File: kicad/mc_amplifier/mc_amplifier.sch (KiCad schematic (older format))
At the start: 19 parts

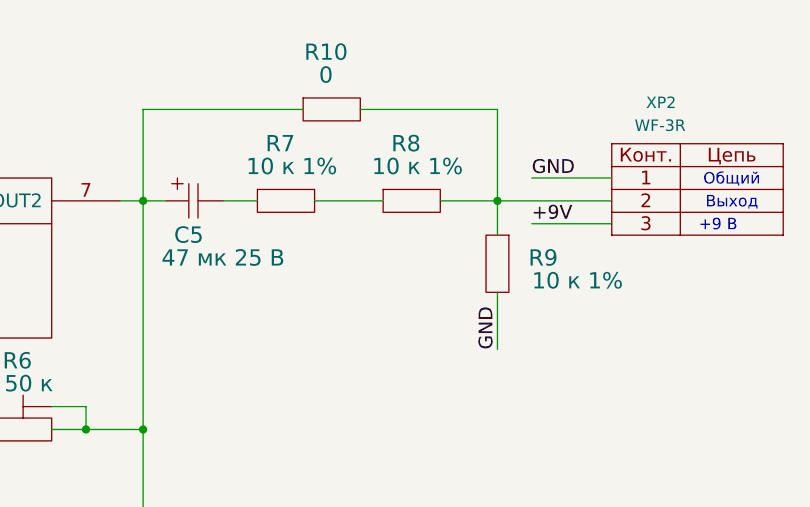
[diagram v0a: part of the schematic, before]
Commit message: Порпвил схему и отравил плату mc_amplifier rev1 на изготовление.
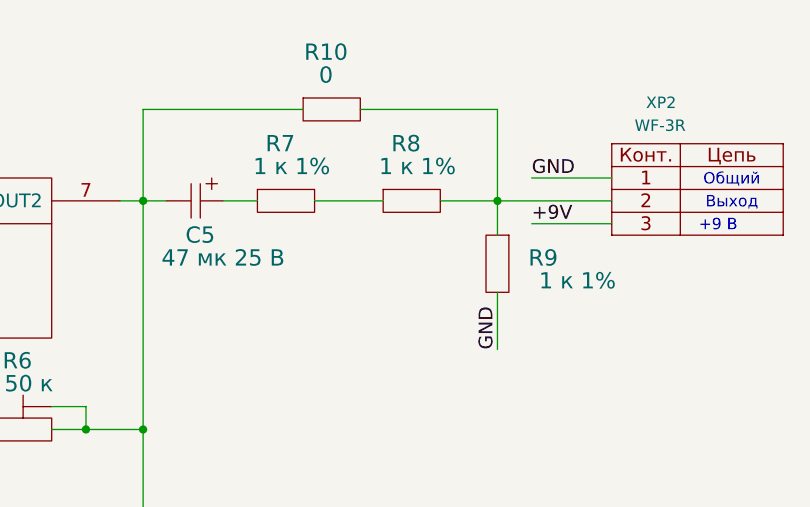
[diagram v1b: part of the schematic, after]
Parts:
- R7, R8, R9: value 10 к 1% -> 1 к 1%
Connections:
- net at C3.1, DA1.7 (OUT2), R10.1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: now also C5.2; no longer C5.1
- net at R7.1: now also C5.1; no longer C5.2
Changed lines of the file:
@@
 L LFcapitors:CAPITORS_ELECTROLYTIC C5
 U 1 1 5DDF39DE
-P 7700 2250
-F 0 "C5" H 7800 2100 71  0000 C CNN
+P 7950 2250
+F 0 "C5" H 8050 2100 71  0000 C CNN
 F 1 "47 мк 25 В" H 7950 2000 71  0000 C CNN
-F 2 "IWsmd_case:CASE_D" H 7700 2250 60  0001 C CNN
-F 3 "" H 7700 2250 60  0000 C CNN
-	1    7700 2250
-	1    0    0    -1
+F 2 "IWsmd_case:CASE_D" H 7950 2250 60  0001 C CNN
+F 3 "" H 7950 2250 60  0000 C CNN
+	1    7950 2250
+	-1   0    0    -1
 $EndComp
 Wire Wire Line
@@
 P 8100 2250
 F 0 "R7" H 8200 2500 71  0000 C CNN
-F 1 "10 к 1%" H 8250 2400 71  0000 C CNN
+F 1 "1 к 1%" H 8250 2400 71  0000 C CNN
 F 2 "IWsmd_case:SMD0805" H 8100 2250 60  0001 C CNN
 F 3 "" H 8225 2481 60  0000 C CNN
@@
 P 8650 2250
 F 0 "R8" H 8750 2500 71  0000 C CNN
-F 1 "10 к 1%" H 8800 2400 71  0000 C CNN
+F 1 "1 к 1%" H 8800 2400 71  0000 C CNN
 F 2 "IWsmd_case:SMD0805" H 8650 2250 60  0001 C CNN
 F 3 "" H 8775 2481 60  0000 C CNN
@@
 P 9150 2400
 F 0 "R9" V 9250 2600 71  0000 C CNN
-F 1 "10 к 1%" V 9350 2750 71  0000 C CNN
+F 1 "1 к 1%" V 9350 2750 71  0000 C CNN
 F 2 "IWsmd_case:SMD0805" H 9150 2400 60  0001 C CNN
 F 3 "" H 9150 2400 60  0000 C CNN

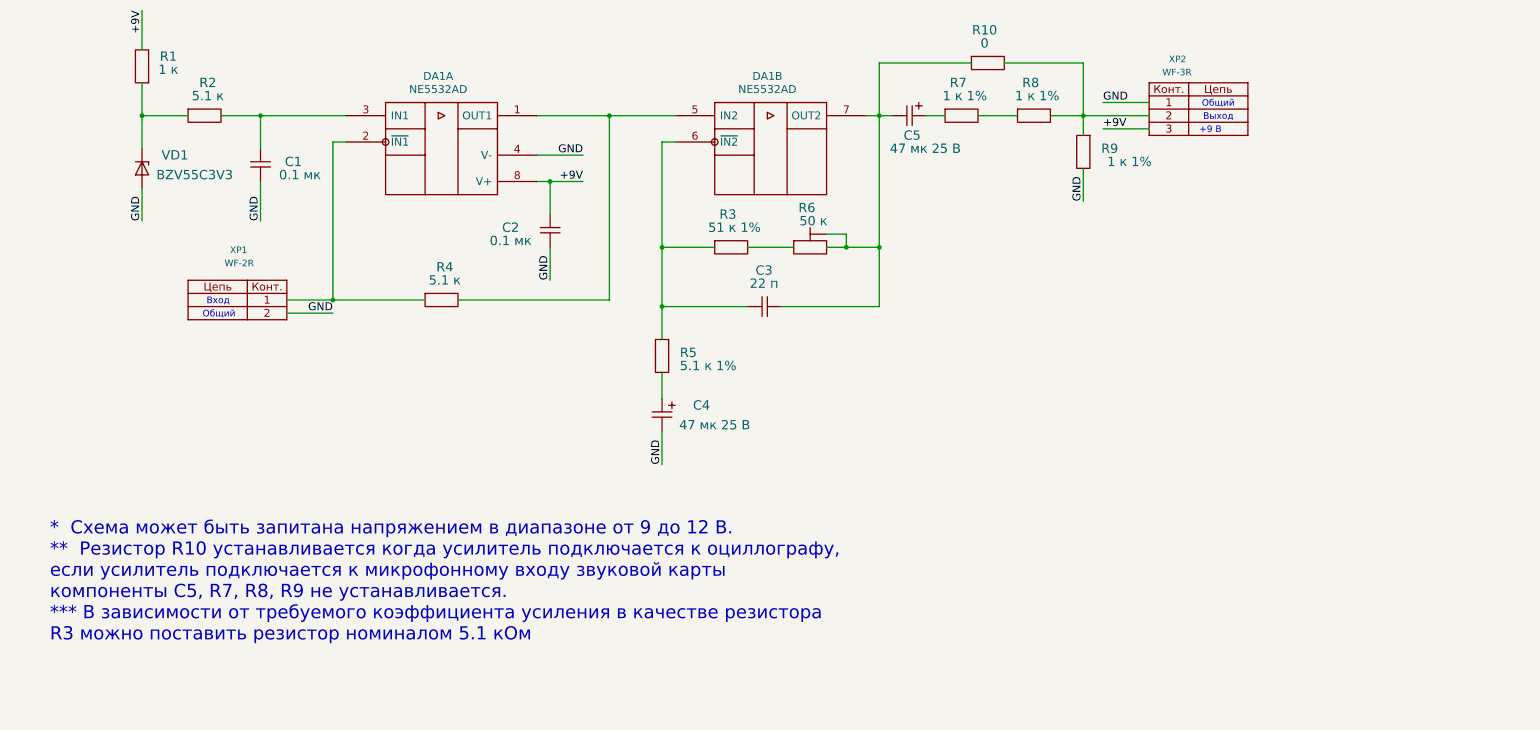
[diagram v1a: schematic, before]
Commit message: Поправил схему и отравил плату mc_amplifier rev1 на изготовление.
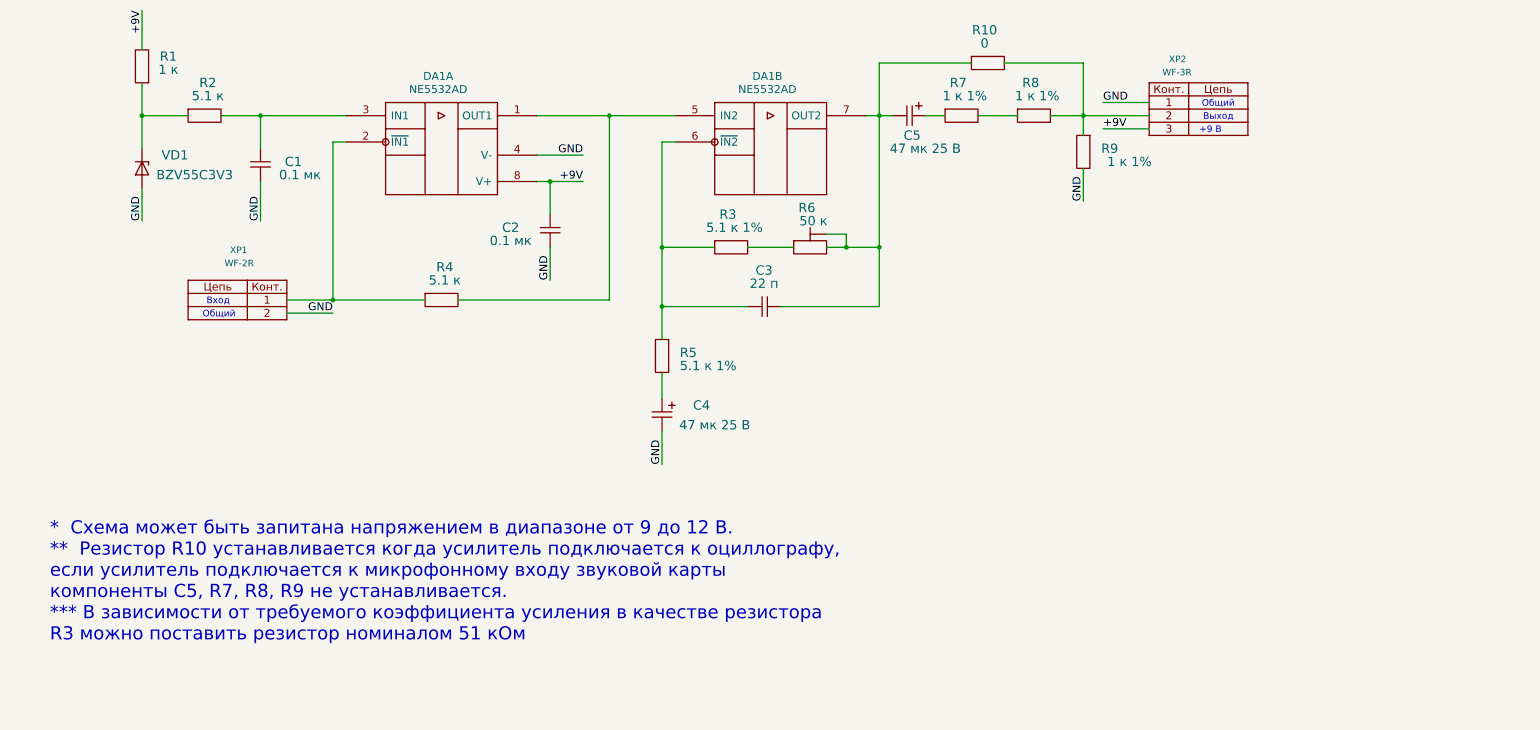
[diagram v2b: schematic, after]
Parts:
- R3: value 51 к 1% -> 5.1 к 1%
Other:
- note added: "* Схема может быть запитана напряжением в диапазоне от 9 до 12 В.\n** Резистор R10 устанавливается когда усилитель подключается к оциллографу,\nесли усилитель подключается к микрофонному входу звуковой карты\nкомпоненты C5, R7, R8, R9 не устанавливается.\n*** В зависимости от требуемого коэффициента усиления в качестве резистора\nR3 можно поставить резистор номиналом 51 кОм"
- note removed: "* Схема может быть запитана напряжением в диапазоне от 9 до 12 В.\n** Резистор R10 устанавливается когда усилитель подключается к оциллографу,\nесли усилитель подключается к микрофонному входу звуковой карты\nкомпоненты C5, R7, R8, R9 не устанавливается.\n*** В зависимости от требуемого коэффициента усиления в качестве резистора\nR3 можно поставить резистор номиналом 5.1 кОм"
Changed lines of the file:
@@
 P 6350 3250
 F 0 "R3" H 6450 3500 71  0000 C CNN
-F 1 "51 к 1%" H 6500 3400 71  0000 C CNN
+F 1 "5.1 к 1%" H 6500 3400 71  0000 C CNN
 F 2 "IWsmd_case:SMD0805" H 6350 3250 60  0001 C CNN
 F 3 "" H 6475 3481 60  0000 C CNN
@@
 	7600 1850 8300 1850
 Text Notes 1300 6250 0    100  ~ 0
-*  Схема может быть запитана напряжением в диапазоне от 9 до 12 В.\n**  Резистор R10 устанавливается когда усилитель подключается к оциллографу,\nесли усилитель подключается к микрофонному входу звуковой карты\nкомпоненты C5, R7, R8, R9 не устанавливается.\n*** В зависимости от требуемого коэффициента усиления в качестве резистора\nR3 можно поставить резистор номиналом 5.1 кОм
+*  Схема может быть запитана напряжением в диапазоне от 9 до 12 В.\n**  Резистор R10 устанавливается когда усилитель подключается к оциллографу,\nесли усилитель подключается к микрофонному входу звуковой карты\nкомпоненты C5, R7, R8, R9 не устанавливается.\n*** В зависимости от требуемого коэффициента усиления в качестве резистора\nR3 можно поставить резистор номиналом 51 кОм
 $EndSCHEMATC

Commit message: Добавил новую ревизию схемы mc_amplifier (rev_2).
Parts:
- added R11: 47 к, IWsmd_case:SMD0805, symbol LFresistor:RESISTOR
- R2, R4: value 5.1 к -> 5.1 к 1%
- R6: value 50 к -> 100 к
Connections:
- net GND: now also R11.2
- net at C3.1, DA1.7 (OUT2), R10.1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: now also R7.1; no longer C5.2
- net at R10.2, XP2.2: now also C5.2, R11.1; no longer R8.2, R9.1
- net at C5.1: now also R8.2, R9.1; no longer R7.1
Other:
- note added: "* Схема может быть запитана напряжением в диапазоне от 9 до 12 В.\nЕсли запитать схему от 15В то на место VD1 нужно поставить стабилитрон BZV55C4V7\n** Резистор R10 устанавливается когда усилитель подключается к оциллографу,\nесли усилитель подключается к микрофонному входу звуковой карты\nкомпоненты C5, R7, R8, R9 должны быть установлены, R10 впаивать не нужно.\n*** Резистор R11 устанавливается 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"
- note removed: "* Схема может быть запитана напряжением в диапазоне от 9 до 12 В.\n** Резистор R10 устанавливается когда усилитель подключается к оциллографу,\nесли усилитель подключается к микрофонному входу звуковой карты\nкомпоненты C5, R7, R8, R9 не устанавливается.\n*** В зависимости от требуемого коэффициента усиления в качестве резистора\nR3 можно поставить резистор номиналом 51 кОм"
- moved on the sheet: C5, R7, R8, R9, XP2
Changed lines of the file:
@@
 Connection ~ 7600 3250
 Wire Wire Line
-	9300 2150 9650 2150
-Text Label 9300 2150 0    60   ~ 0
+	9600 2150 9950 2150
+Text Label 9600 2150 0    60   ~ 0
 GND
 Wire Wire Line
-	9300 2350 9650 2350
-Text Label 9300 2350 0    60   ~ 0
+	9600 2350 9950 2350
+Text Label 9600 2350 0    60   ~ 0
 +9V
 $Comp
@@
 P 2350 2250
 F 0 "R2" H 2500 2500 71  0000 C CNN
-F 1 "5.1 к" H 2500 2400 71  0000 C CNN
+F 1 "5.1 к 1%" H 2500 2400 71  0000 C CNN
 F 2 "IWsmd_case:SMD0805" H 2350 2250 60  0001 C CNN
 F 3 "" H 2350 2250 60  0000 C CNN
@@
 P 4150 3650
 F 0 "R4" H 4300 3900 71  0000 C CNN
-F 1 "5.1 к" H 4300 3800 71  0000 C CNN
+F 1 "5.1 к 1%" H 4300 3800 71  0000 C CNN
 F 2 "IWsmd_case:SMD0805" H 4150 3650 60  0001 C CNN
 F 3 "" H 4150 3650 60  0000 C CNN
@@
 L LFconnectors:connector_3pin_gost XP2
 U 1 1 53E88414
-P 9650 2150
-F 0 "XP2" H 9800 2450 50  0000 L BNN
-F 1 "WF-3R" H 9750 2350 50  0000 L BNN
-F 2 "IWconnectors:WF-3" H 10100 2300 50  0001 C CNN
-F 3 "" H 9650 2150 60  0000 C CNN
-	1    9650 2150
+P 9950 2150
+F 0 "XP2" H 10100 2450 50  0000 L BNN
+F 1 "WF-3R" H 10050 2350 50  0000 L BNN
+F 2 "IWconnectors:WF-3" H 10400 2300 50  0001 C CNN
+F 3 "" H 9950 2150 60  0000 C CNN
+	1    9950 2150
 	1    0    0    -1
 $EndComp
@@
 P 6950 3250
 F 0 "R6" H 7050 3550 71  0000 C CNN
-F 1 "50 к" H 7100 3450 71  0000 C CNN
+F 1 "100 к" H 7100 3450 71  0000 C CNN
 F 2 "IWsmd_case:BOURNS_3224J" H 6950 3250 60  0001 C CNN
 F 3 "" H 7075 3481 60  0000 C CNN
@@
 Text Notes 2460 3790 0    50   ~ 0
 Общий
-Text Notes 10060 2290 0    50   ~ 0
+Text Notes 10360 2290 0    50   ~ 0
 Выход
-Text Notes 10030 2390 0    50   ~ 0
+Text Notes 10330 2390 0    50   ~ 0
  +9 В
-Text Notes 10050 2190 0    50   ~ 0
+Text Notes 10350 2190 0    50   ~ 0
 Общий
 $Comp
 L LFcapitors:CAPITORS_ELECTROLYTIC C5
 U 1 1 5DDF39DE
-P 7950 2250
-F 0 "C5" H 8050 2100 71  0000 C CNN
-F 1 "47 мк 25 В" H 7950 2000 71  0000 C CNN
-F 2 "IWsmd_case:CASE_D" H 7950 2250 60  0001 C CNN
-F 3 "" H 7950 2250 60  0000 C CNN
-	1    7950 2250
-	-1   0    0    -1
-$EndComp
-Wire Wire Line
-	7700 2250 7600 2250
+P 9000 2250
+F 0 "C5" H 9100 2550 71  0000 C CNN
+F 1 "47 мк 25 В" H 9100 2450 71  0000 C CNN
+F 2 "IWsmd_case:CASE_D" H 9000 2250 60  0001 C CNN
+F 3 "" H 9000 2250 60  0000 C CNN
+	1    9000 2250
+	1    0    0    -1
+$EndComp
 Connection ~ 7600 2250
 $Comp
 L LFresistor:RESISTOR R7
 U 1 1 5DDFC765
-P 8100 2250
-F 0 "R7" H 8200 2500 71  0000 C CNN
-F 1 "1 к 1%" H 8250 2400 71  0000 C CNN
-F 2 "IWsmd_case:SMD0805" H 8100 2250 60  0001 C CNN
-F 3 "" H 8225 2481 60  0000 C CNN
-	1    8100 2250
+P 7750 2250
+F 0 "R7" H 7850 2500 71  0000 C CNN
+F 1 "1 к 1%" H 7900 2400 71  0000 C CNN
+F 2 "IWsmd_case:SMD0805" H 7750 2250 60  0001 C CNN
+F 3 "" H 7875 2481 60  0000 C CNN
+	1    7750 2250
 	1    0    0    -1
 $EndComp
@@
 L LFresistor:RESISTOR R8
 U 1 1 5DE0141A
-P 8650 2250
-F 0 "R8" H 8750 2500 71  0000 C CNN
-F 1 "1 к 1%" H 8800 2400 71  0000 C CNN
-F 2 "IWsmd_case:SMD0805" H 8650 2250 60  0001 C CNN
-F 3 "" H 8775 2481 60  0000 C CNN
-	1    8650 2250
-	1    0    0    -1
-$EndComp
-Wire Wire Line
-	7950 2250 8100 2250
-Wire Wire Line
-	8350 2250 8650 2250
-Wire Wire Line
-	8900 2250 9150 2250
+P 8300 2250
+F 0 "R8" H 8400 2500 71  0000 C CNN
+F 1 "1 к 1%" H 8450 2400 71  0000 C CNN
+F 2 "IWsmd_case:SMD0805" H 8300 2250 60  0001 C CNN
+F 3 "" H 8425 2481 60  0000 C CNN
+	1    8300 2250
+	1    0    0    -1
+$EndComp
+Wire Wire Line
+	7600 2250 7750 2250
+Wire Wire Line
+	8000 2250 8300 2250
+Wire Wire Line
+	8550 2250 8800 2250
 $Comp
 L LFresistor:RESISTOR R9
 U 1 1 5DE0763D
-P 9150 2400
-F 0 "R9" V 9250 2600 71  0000 C CNN
-F 1 "1 к 1%" V 9350 2750 71  0000 C CNN
-F 2 "IWsmd_case:SMD0805" H 9150 2400 60  0001 C CNN
-F 3 "" H 9150 2400 60  0000 C CNN
-	1    9150 2400
-	0    1    1    0
-$EndComp
-Wire Wire Line
-	9150 2250 9150 2400
-Connection ~ 9150 2250
-Wire Wire Line
-	9150 2250 9650 2250
-Wire Wire Line
-	9150 2650 9150 2900
-Text Label 9150 2900 1    60   ~ 0
+P 8800 2400
+F 0 "R9" V 8900 2600 71  0000 C CNN
+F 1 "1 к 1%" V 9000 2700 71  0000 C CNN
+F 2 "IWsmd_case:SMD0805" H 8800 2400 60  0001 C CNN
+F 3 "" H 8800 2400 60  0000 C CNN
+	1    8800 2400
+	0    1    1    0
+$EndComp
+Wire Wire Line
+	8800 2250 8800 2400
+Wire Wire Line
+	8800 2650 8800 2900
+Text Label 8800 2900 1    60   ~ 0
 GND
 $Comp
@@
 $EndComp
 Wire Wire Line
-	9150 2250 9150 1850
-Wire Wire Line
-	9150 1850 8550 1850
-Wire Wire Line
 	7600 2250 7600 1850
 Wire Wire Line
 	7600 1850 8300 1850
 Text Notes 1300 6250 0    100  ~ 0
-*  Схема может быть запитана напряжением в диапазоне от 9 до 12 В.\n**  Резистор R10 устанавливается когда усилитель подключается к оциллографу,\nесли усилитель подключается к микрофонному входу звуковой карты\nкомпоненты C5, R7, R8, R9 не устанавливается.\n*** В зависимости от требуемого коэффициента усиления в качестве резистора\nR3 можно поставить резистор номиналом 51 кОм
+*  Схема может быть запитана напряжением в диапазоне от 9 до 12 В.\nЕсли запитать схему от 15В то на место VD1 нужно поставить стабилитрон BZV55C4V7\n**  Резистор R10 устанавливается когда усилитель подключается к оциллографу,\nесли усилитель подключается к микрофонному входу звуковой карты\nкомпоненты C5, R7, R8, R9 должны быть установлены, R10 впаивать не нужно.\n*** Резистор R11 устанавливается в зависимости от необходимости.
+Wire Wire Line
+	8800 2250 9000 2250
+Connection ~ 8800 2250
+Wire Wire Line
+	9250 2250 9450 2250
+Wire Wire Line
+	9450 2250 9450 1850
+Wire Wire Line
+	8550 1850 9450 1850
+Wire Wire Line
+	9450 2250 9950 2250
+Connection ~ 9450 2250
+$Comp
+L LFresistor:RESISTOR R11
+U 1 1 5E1CCD8B
+P 9450 2400
+F 0 "R11" V 9550 2600 71  0000 C CNN
+F 1 "47 к" V 9650 2600 71  0000 C CNN
+F 2 "IWsmd_case:SMD0805" H 9450 2400 60  0001 C CNN
+F 3 "" H 9450 2400 60  0000 C CNN
+	1    9450 2400
+	0    1    1    0
+$EndComp
+Wire Wire Line
+	9450 2250 9450 2400
+Wire Wire Line
+	9450 2650 9450 2900
+Text Label 9450 2900 1    60   ~ 0
+GND
 $EndSCHEMATC

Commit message: Проверил работоспособность платы mc_amplifier ver_1.
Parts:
- removed R11: 47 к, IWsmd_case:SMD0805, symbol LFresistor:RESISTOR
- R2: value 5.1 к 1% -> 5.1 к
- R3, R5: value 5.1 к 1% -> 1 к 1%
- R6: value 100 к -> 50 к
- R7, R8, R9: value 1 к 1% -> 10 к 1%
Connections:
- net at C3.1, DA1.7 (OUT2), R10.1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: now also C5.2; no longer R7.1
- net at R10.2, XP2.2: now also R8.2, R9.1; no longer C5.2
- new net: C5.1, R7.1
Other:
- note added: "* Схема может быть запитана напряжением в диапазоне от 9 до 15 В.\n Если напряжения питания усилителя 15 В то необходимо заменить стабилитрон\n VD1 с BZV55C3V3 на BZV55C4V7.\n\n** Резистор R10 устанавливается когда усилитель подключается к оциллографу.\n Если усилитель подключается к микрофонному входу звуковой карты то\n необходимо установить разделительный конденсатор C5 и делить напряжения 1:3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"
- note added: "+!!!"
- note removed: "* Схема может быть запитана напряжением в диапазоне от 9 до 12 В.\nЕсли запитать схему от 15В то на место VD1 нужно поставить стабилитрон BZV55C4V7\n** Резистор R10 устанавливается когда усилитель подключается к оциллографу,\nесли усилитель подключается к микрофонному входу звуковой карты\nкомпоненты C5, R7, R8, R9 должны быть установлены, R10 впаивать не нужно.\n*** Резистор R11 устанавливается 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"
- moved on the sheet: C5, R7, R8, R9, XP2
